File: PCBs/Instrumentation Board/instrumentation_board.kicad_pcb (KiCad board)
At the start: 2 copper layers, 65 x 102 mm, 57 parts, among them J1 Conn_01x02, J2 Conn_01x02, J3 Conn_01x02, J4 Conn_01x02, J5 Conn_01x02, Q1 TEMT6000X01, U1 GPS-ADAFRUIT746, U10 PI4ULS5V201TAEX, U11 PI4ULS5V201TAEX, U12 PI4ULS5V201TAEX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

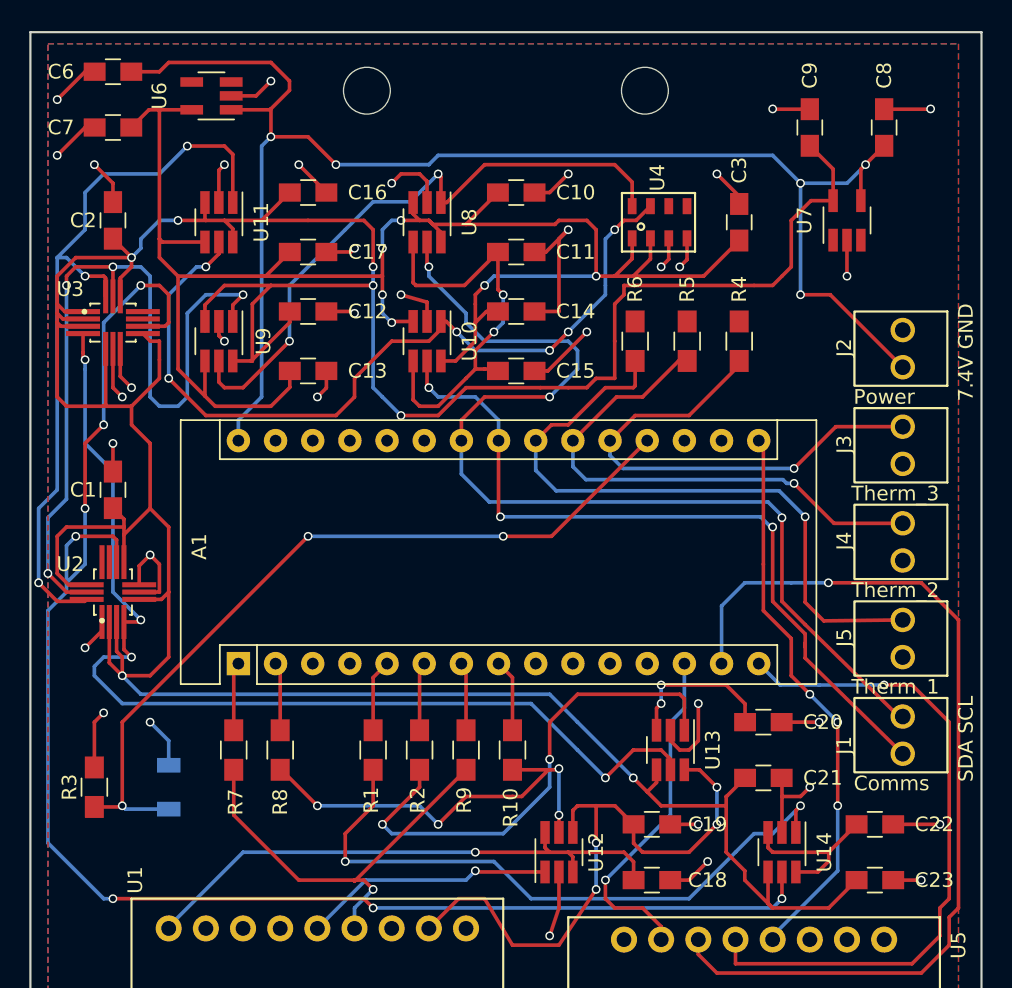
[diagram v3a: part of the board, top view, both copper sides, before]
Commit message: fixed some outstanding instr issues, removed lots of vias
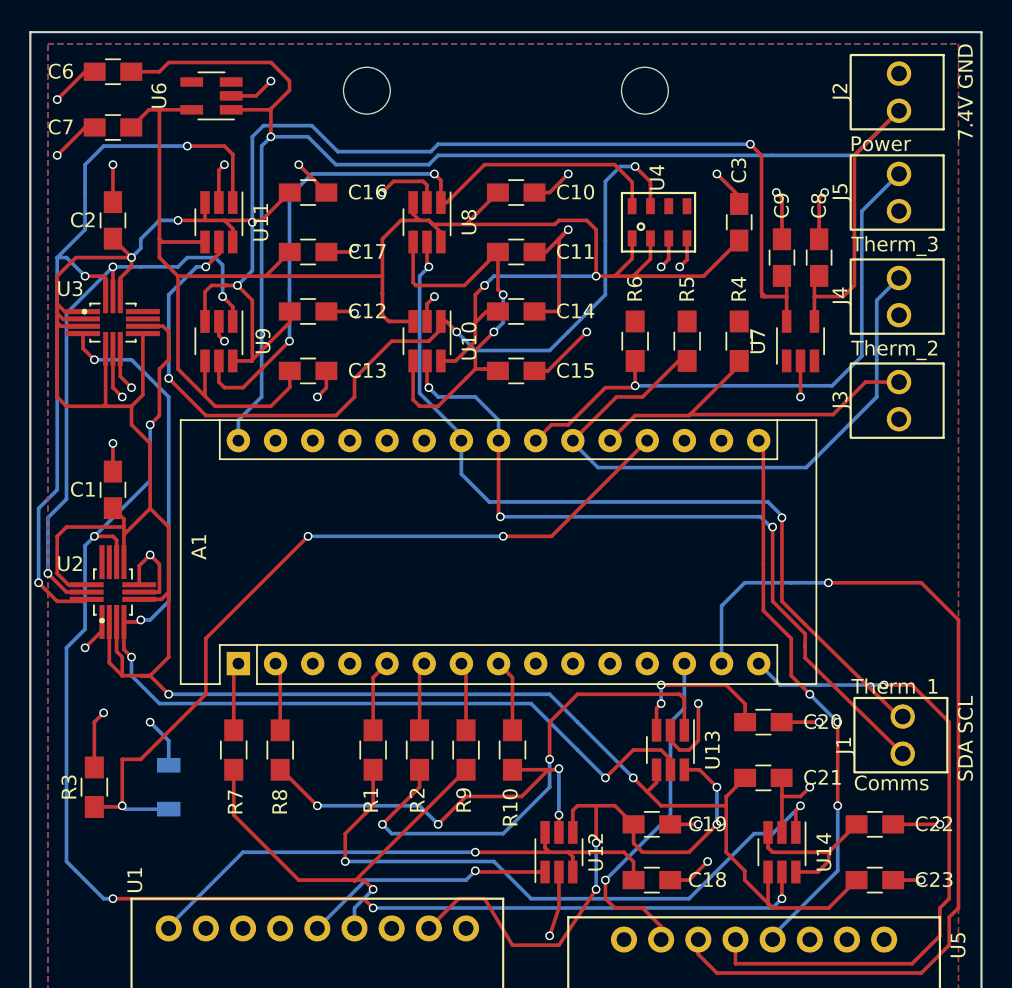
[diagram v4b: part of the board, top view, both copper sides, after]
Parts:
- moved J5 30.5 mm to (137.4, 61.0)
- moved J2 17.5 mm to (137.4, 54.1)
- moved J4 16.8 mm to (137.4, 68.1)
- moved C8 9.94 mm to (128.9, 65.4)
- moved C9 9.09 mm to (126.4, 65.4)
- moved U7 8.84 mm to (127.6, 71.1)
- moved J3 3.06 mm to (137.4, 75.2)
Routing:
- net 1.8V: track 263.1 -> 247.0 mm
- net SCL_1.8V: track 55.8 -> 40.1 mm, vias 4 -> 3
- net INT1_1.8V: track 108.6 -> 96.4 mm, vias 7 -> 5
- net SCL_5V: track 70.0 -> 58.0 mm, vias 3 -> 2
- net /Sheet5ABF9899_2/THERM_OUT: track 34.2 -> 26.8 mm, vias 1 -> 0
- net /Sheet5ABF9899/THERM_OUT: track 36.2 -> 42.6 mm, vias 1 -> 0
- net SDA_3V: track 55.9 -> 61.5 mm, vias 6 -> 4
- net /Sheet5ABF9899_3/THERM_OUT: track 44.8 -> 39.9 mm
- net SCL_3V: track 43.2 -> 46.6 mm
- net INT0_1.8V: track 72.5 -> 71.2 mm
- net SDA_1.8V: track 51.9 -> 53.0 mm
- net SIG: track 54.8 -> 55.6 mm
- net 7.4V: track 104.5 -> 105.1 mm, vias 5 -> 1
- net 3V: track 122.3 -> 121.8 mm, vias 6 -> 2

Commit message: fixed outstanding changes on instr and transponder board
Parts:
- U4: footprint SMD:8-SMD -> SMD:8-SMD-Handsolder
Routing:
- net 5V: track 95.1 -> 61.0 mm, vias 9 -> 3
- net 1.8V: track 247.0 -> 277.7 mm
- net INT1_5V: track 43.8 -> 73.4 mm
- net MISO: track 46.0 -> 19.5 mm, vias 1 -> 0
- net INT1_1.8V: track 96.4 -> 117.8 mm, vias 5 -> 3
- net GND: track 117.6 -> 100.8 mm
- net INT0_5V: track 34.5 -> 22.5 mm, vias 2 -> 4
- net GPS_IN: track 28.8 -> 36.9 mm, vias 1 -> 0
- net MOSI: track 63.8 -> 58.5 mm
- net SLK: track 38.2 -> 42.2 mm, vias 3 -> 1
- net /Sheet5ABF9899/THERM_OUT: track 42.6 -> 46.3 mm
- net GPS_OUT: track 29.6 -> 26.4 mm, vias 4 -> 2
- net SCL_1.8V: track 40.1 -> 41.7 mm
- net SDA_3V: track 61.5 -> 60.6 mm
- net SIG: track 55.6 -> 54.8 mm, vias 3 -> 1
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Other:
- rule pad_to_mask_clearance: 0.002 -> 25.4

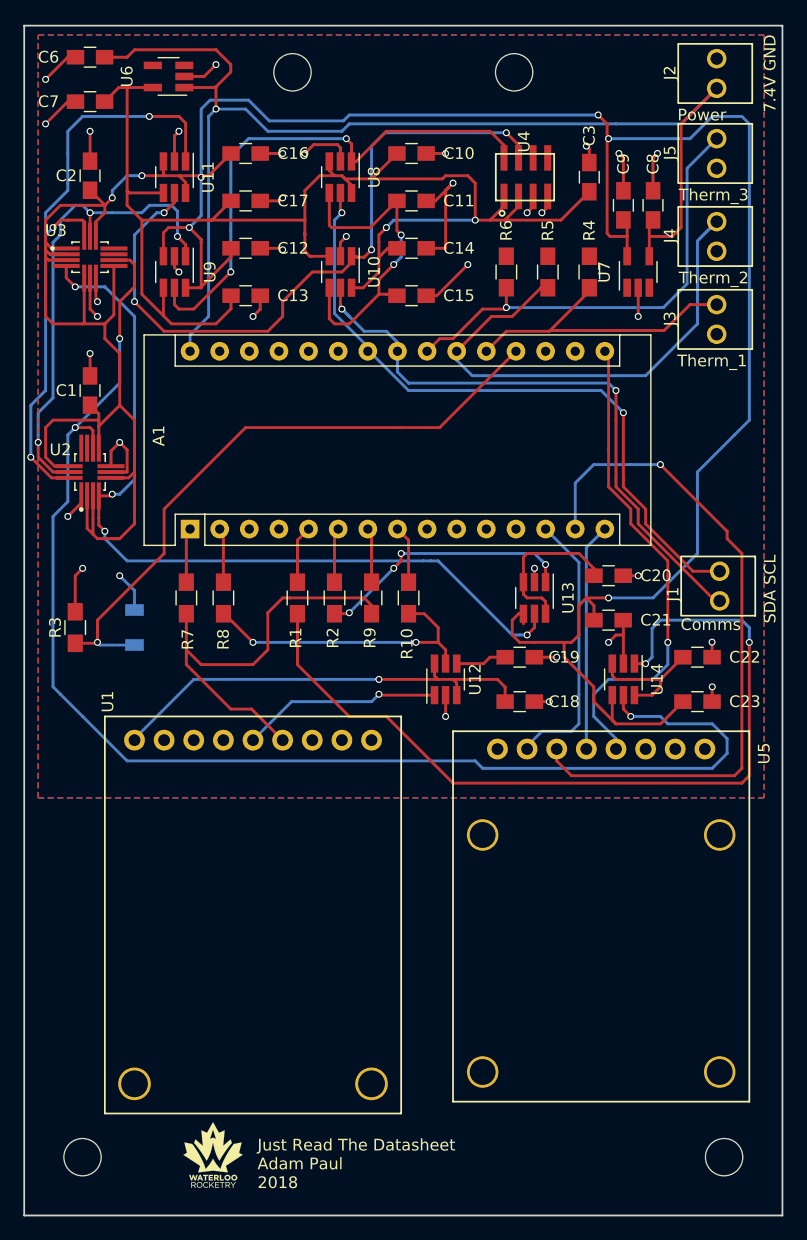
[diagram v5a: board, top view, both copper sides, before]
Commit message: swapped all mounting holes with plated ones, fixed disconnected components on recovery, added the 4 decoupling caps to recovery, fixed silk screen on pads in instr, fixed traces connecting through pads on recovery and instr, moved q1 on instr, brought trace in near u2 on instr, switched u2 & u3 to hand solder on instr, fixed xbee screen on recovery, fixed connector labels on recovery, removed recovery dims past edge cuts, fixed pad mask clearance on recovery
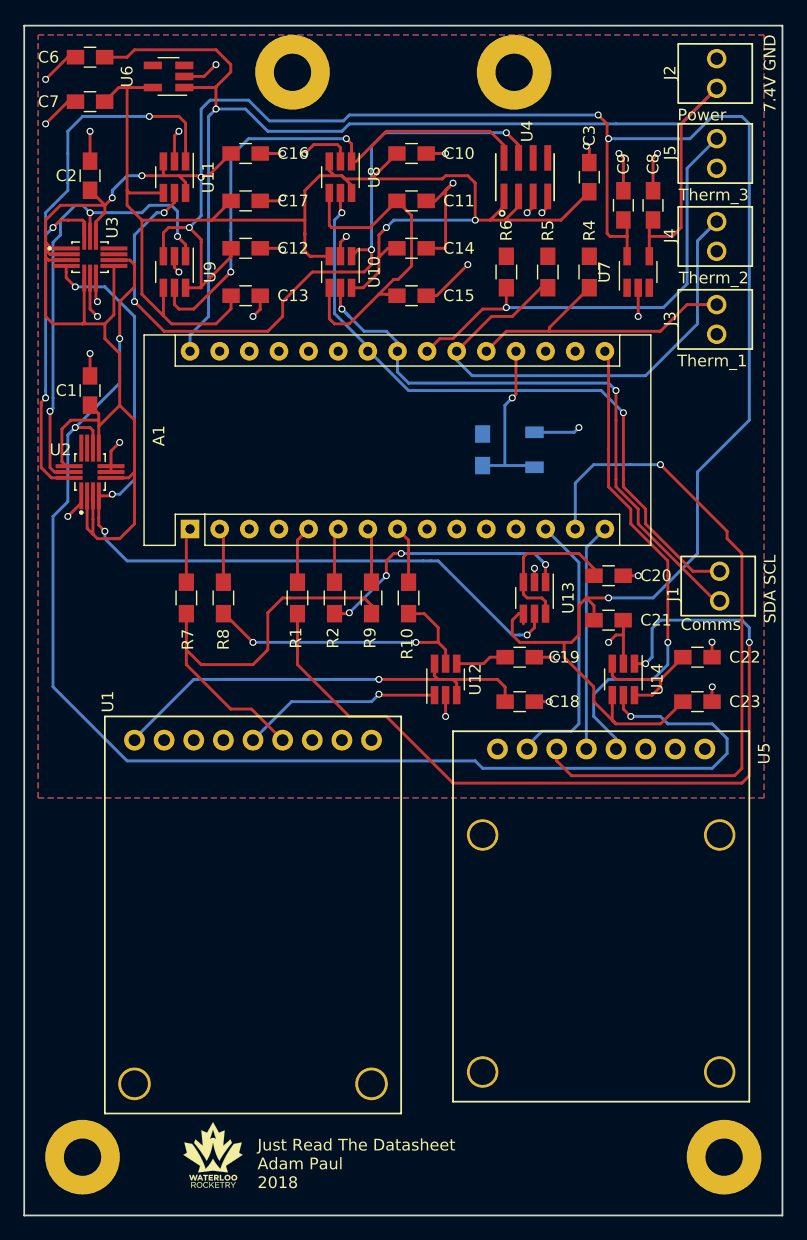
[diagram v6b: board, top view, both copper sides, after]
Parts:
- R3: moved to B.Cu
- REF** (x4): footprint Mounting_Holes:MountingHole_3.2mm_M3 -> Mounting_Holes:MountingHole_3.2mm_M3_Pad
- moved R3 38.1 mm to (114.3, 86.4)
- moved Q1 37.5 mm to (118.7, 86.4)
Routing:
- net SIG: track 54.8 -> 14.8 mm
- net GND: track 100.8 -> 93.1 mm, vias 35 -> 34
- net SDA_3V: track 60.6 -> 63.4 mm
- net 1.8V: track 277.7 -> 275.0 mm
- net 5V: track 61.0 -> 62.5 mm, vias 3 -> 1
- net SCL_1.8V: track 41.7 -> 40.8 mm
- net SDA_1.8V: track 52.6 -> 51.8 mm

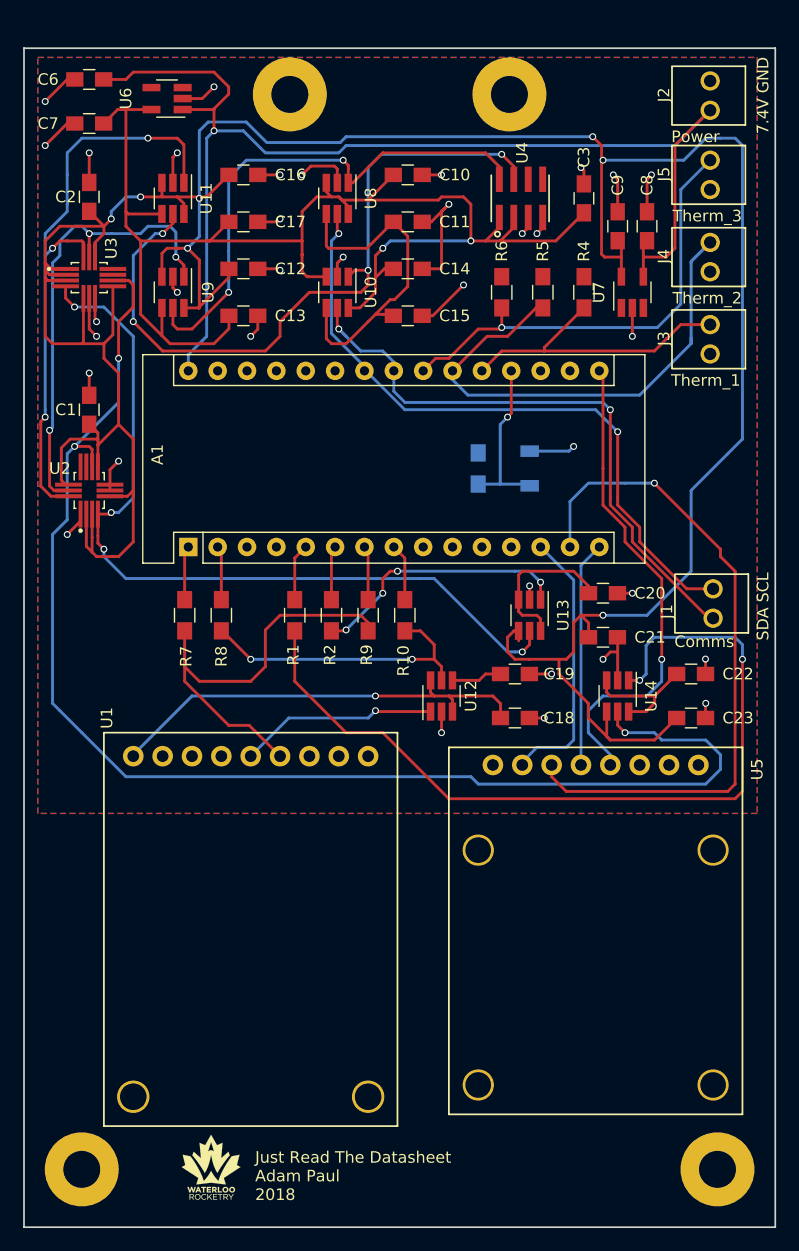
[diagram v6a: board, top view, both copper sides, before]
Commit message: Changes to instr connectors
Extended instr board length
moved power connector to top of board
removed I2C connector to top of board
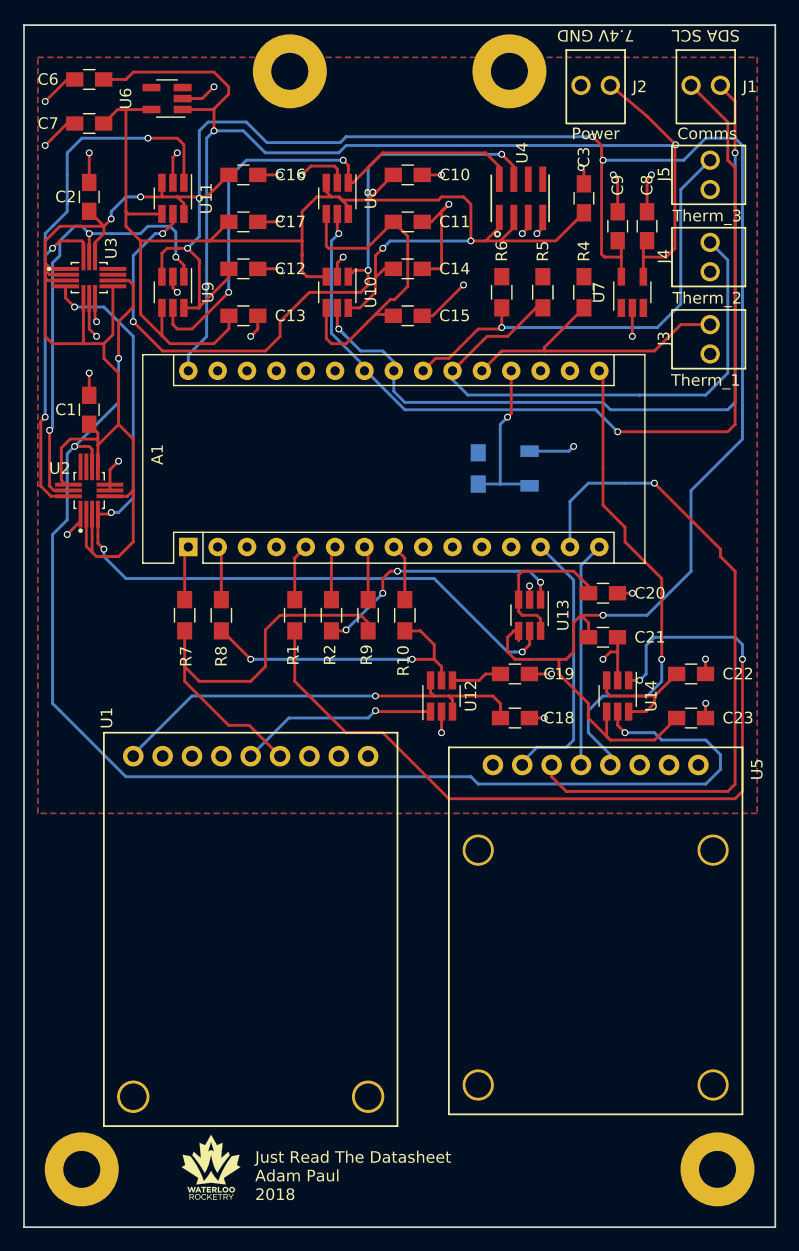
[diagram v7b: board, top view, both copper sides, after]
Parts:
- moved J1 48.0 mm to (134.0, 50.2), turned to 180 degrees
- moved J2 13.5 mm to (124.5, 50.2), turned to 180 degrees
- moved REF** 2.00 mm to (117.0, 52.0)
- moved REF** 2.00 mm to (98.0, 52.0)
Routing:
- net SCL_5V: track 57.9 -> 80.7 mm
- net SDA_5V: track 53.4 -> 70.4 mm
- net /Sheet5ABF9899/THERM_OUT: track 46.3 -> 48.2 mm
- net 7.4V: track 105.1 -> 104.3 mm, vias 1 -> 2
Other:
- board size 65 x 102 mm -> 65 x 104 mm

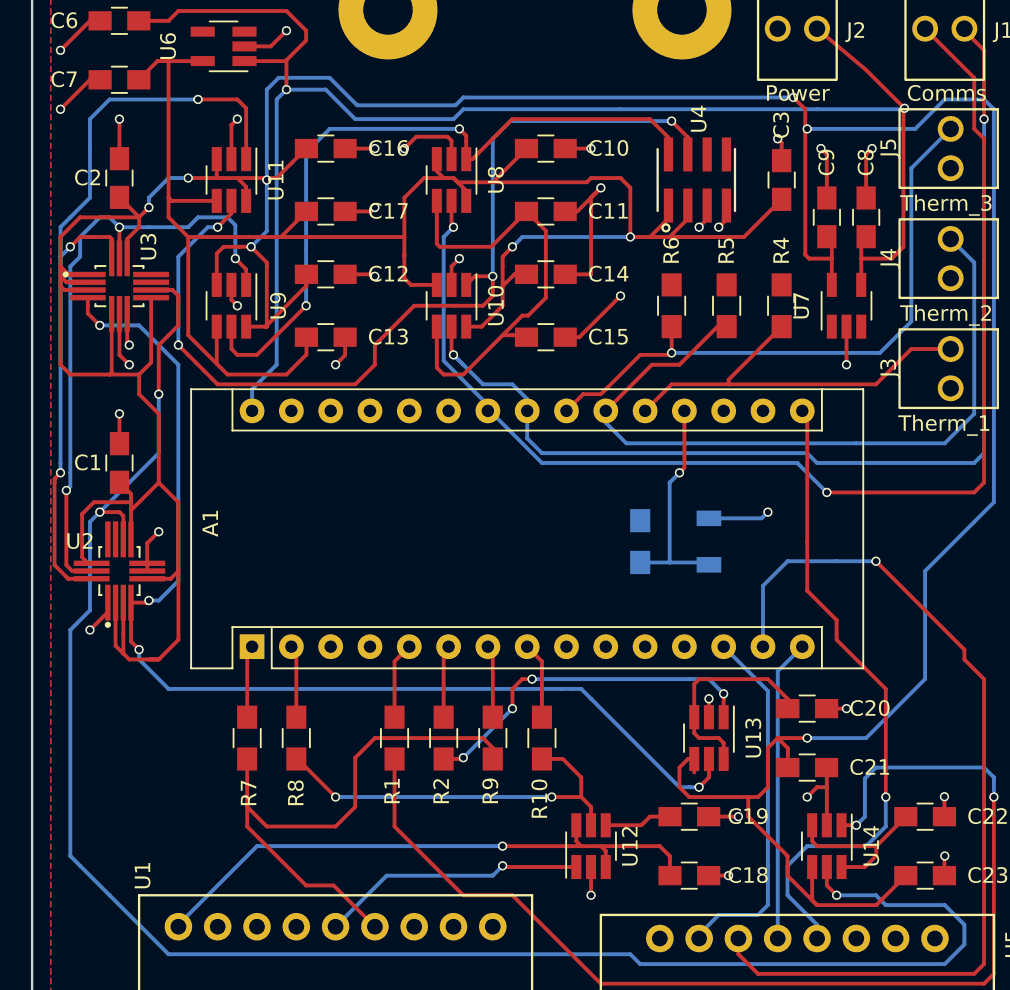
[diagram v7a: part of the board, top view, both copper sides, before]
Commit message: Fixed instr and recovery components per Alexs review
Added IMU current limiting resistors
Moved the caps near J4 on instr
Swapped out phototransistor footprint
Flipped I2C silk screen on J1 recovery
Flipped GND and TX silk screen on J6 recovery
renamed strat to alt on recovery silk screen
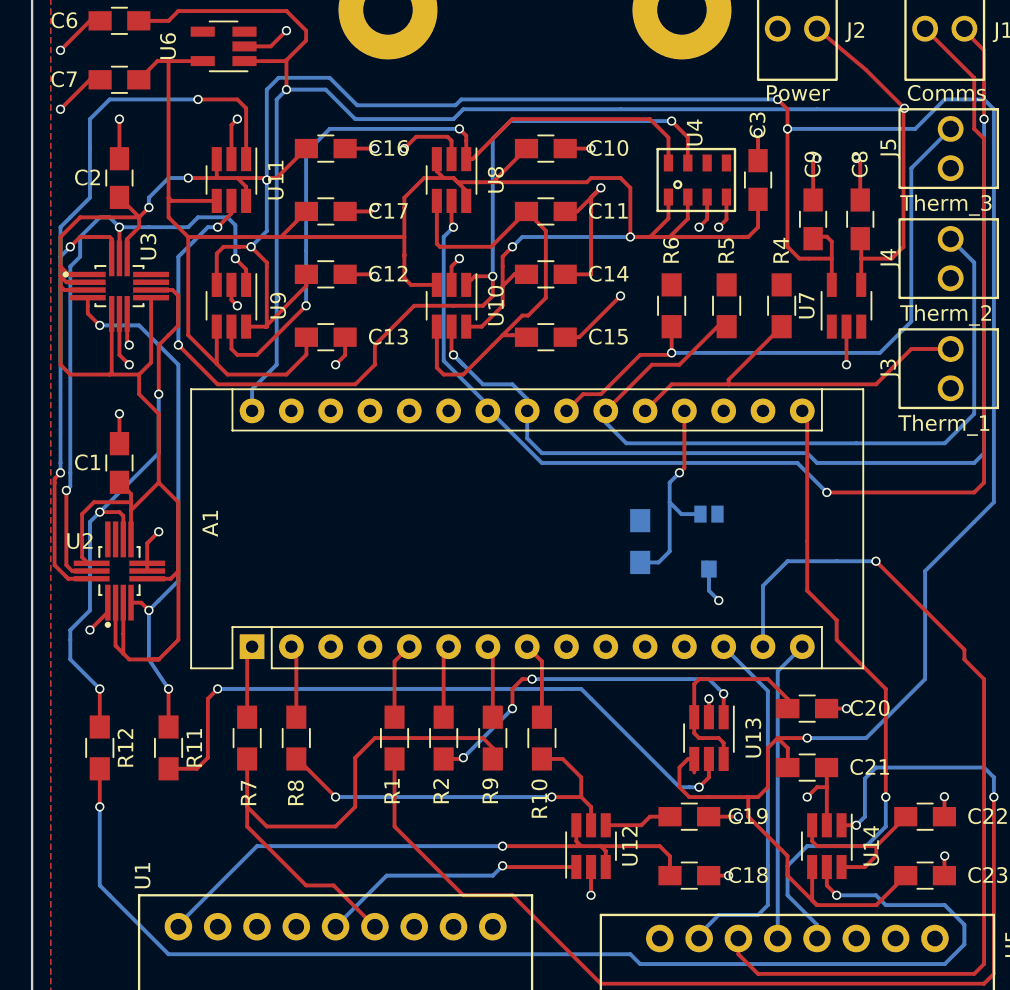
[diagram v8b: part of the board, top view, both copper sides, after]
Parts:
- added R11: 450, Resistors_SMD:R_0805_HandSoldering, F.Cu at (83.8, 99.7)
- added R12: 450, Resistors_SMD:R_0805_HandSoldering, F.Cu at (79.4, 99.7)
- Q1: footprint Diodes_SMD:D_1206 -> TEMT6000X01:TEMT6000X01
- U4: footprint SMD:8-SMD-Handsolder -> SMD:8-SMD
- moved C3 1.52 mm to (121.9, 63.0)
- moved C9 0.90 mm to (125.5, 65.5)
- moved C8 0.40 mm to (128.5, 65.5)
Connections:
- U13 pad 5: INT0_1.8V -> /ICShifter5/B
- U14 pad 5: INT1_1.8V -> /ICShifter6/B
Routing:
- net INT1_1.8V: track 117.8 -> 36.6 mm
- net /ICShifter6/B: track 0.00 -> 78.5 mm, vias 0 -> 2
- net /ICShifter5/B: track 0.00 -> 43.4 mm, vias 0 -> 2
- net INT0_1.8V: track 71.4 -> 34.2 mm, vias 4 -> 3
- net GND: track 93.1 -> 91.1 mm
- net 1.8V: track 275.0 -> 276.7 mm
- net 5V: track 62.5 -> 61.0 mm
- net SIG: track 14.8 -> 14.0 mm
